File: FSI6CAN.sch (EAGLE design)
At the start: 32 parts, among them IC1 ATMEGA32M1, IC2 MCP2551

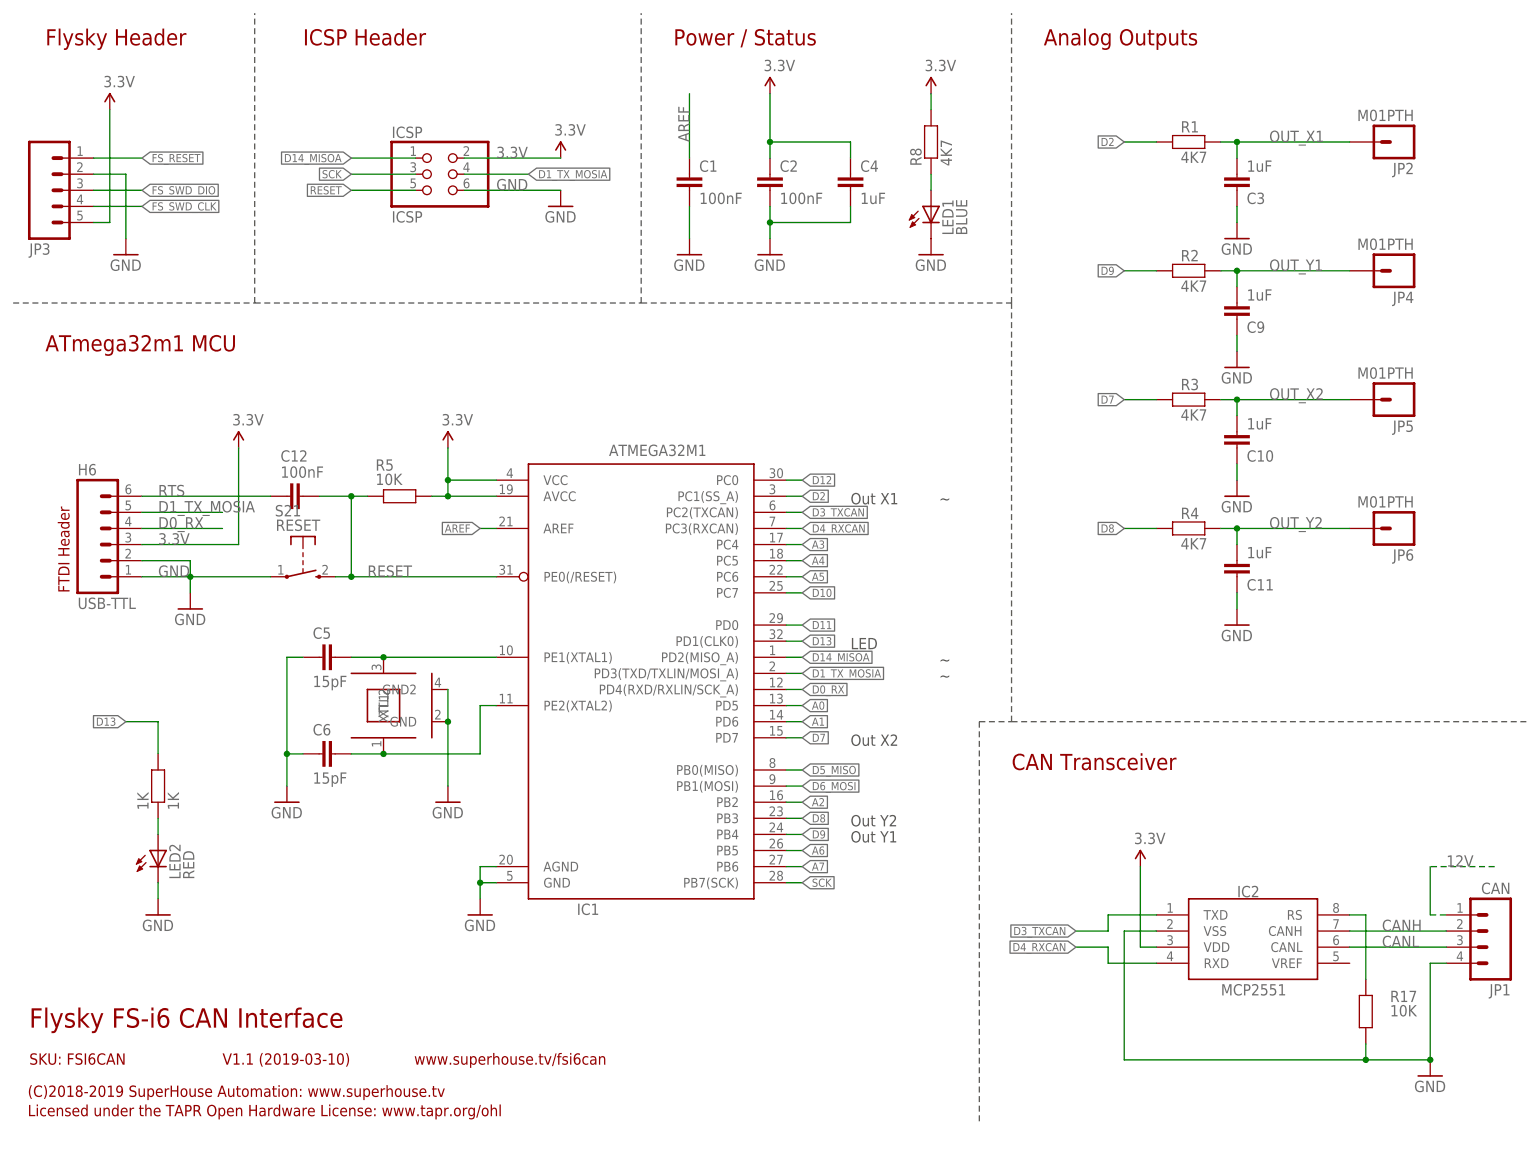
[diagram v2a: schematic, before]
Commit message: Added CAN termination
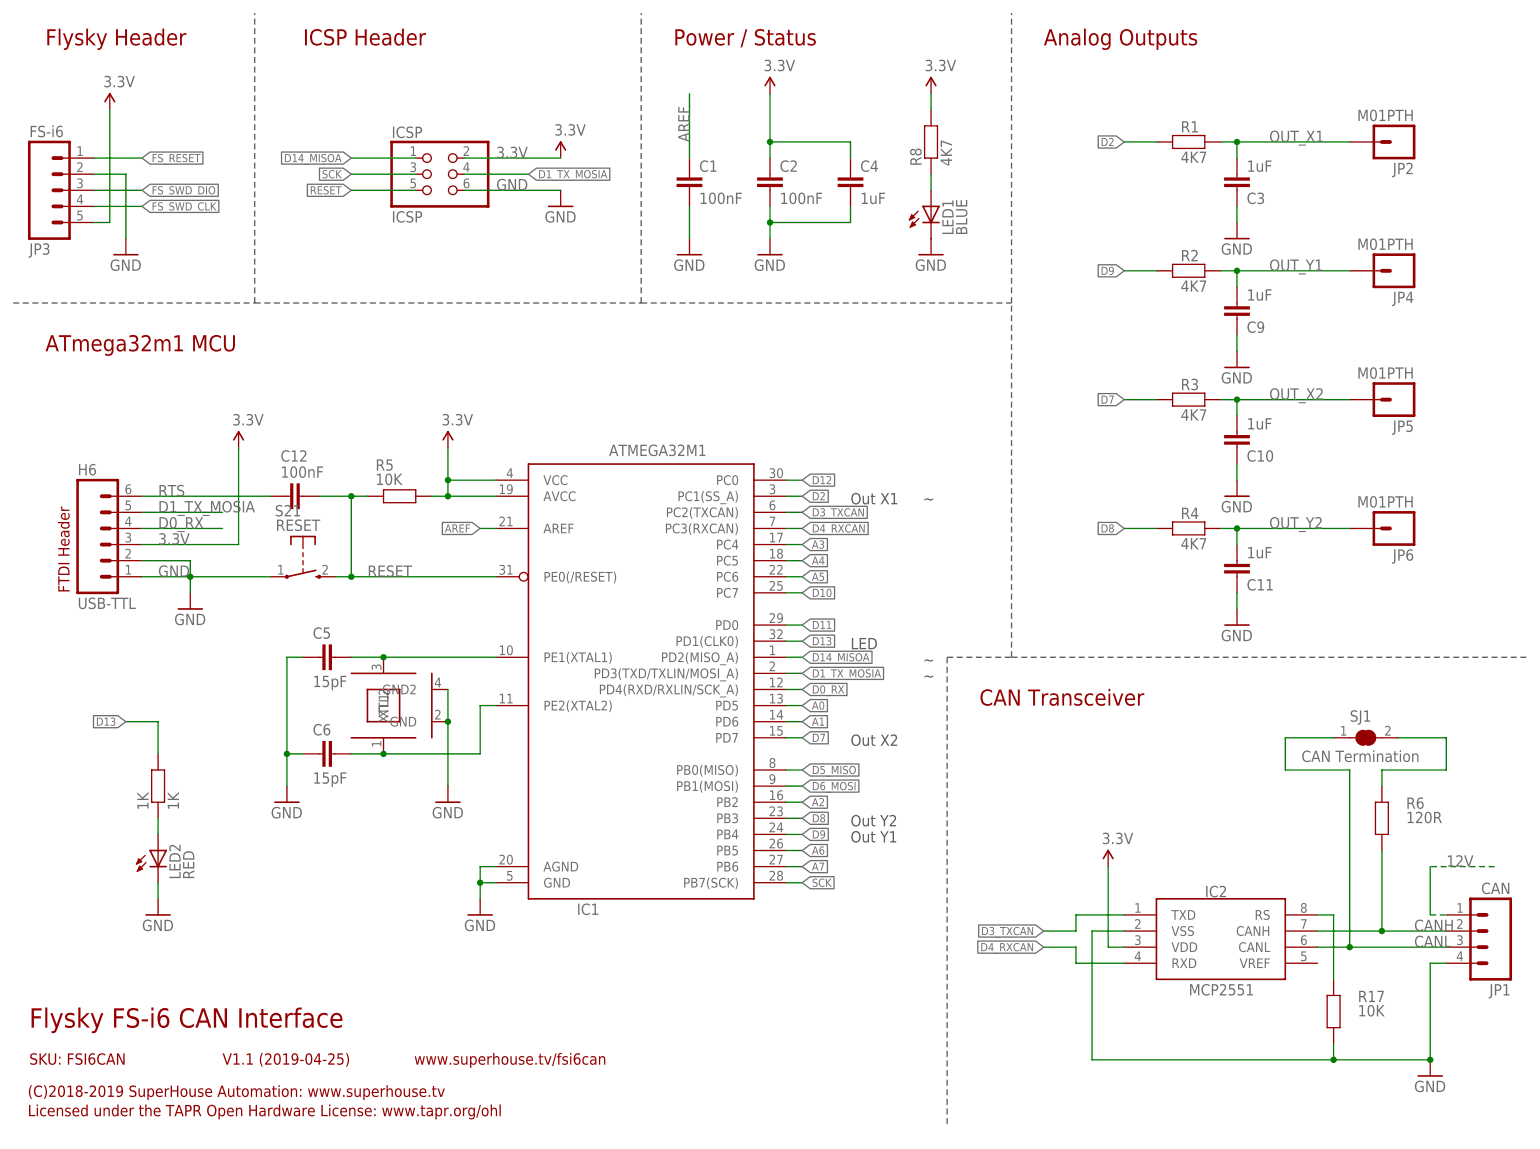
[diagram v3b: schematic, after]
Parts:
- added R6: 120R, freetronics-master-v1.1:RESISTOR0603
- added SJ1: CAN Termination, freetronics-jon:SJCN
- JP3: value (none) -> FS-i6
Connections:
- new net N$2: R6.2, SJ1.2
- net CANH: now also R6.1
- net CANL: now also SJ1.1
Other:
- note added: "V1.1 (2019-04-25)"
- note removed: "V1.1 (2019-03-10)"
- moved on the sheet: IC2, R17

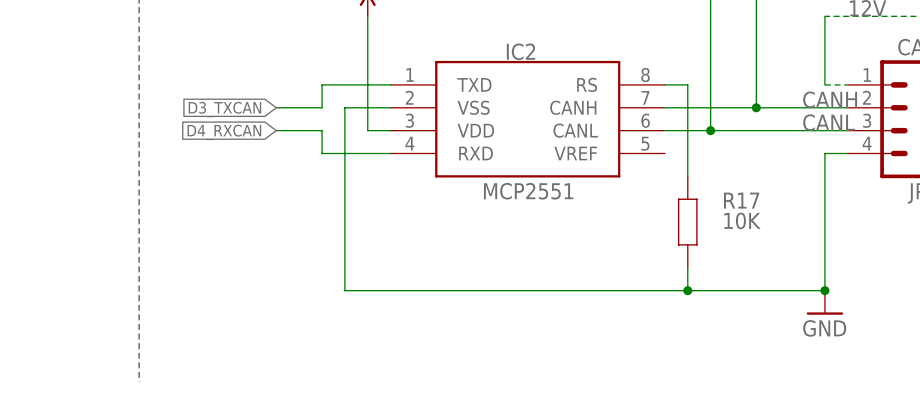
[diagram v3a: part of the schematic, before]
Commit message: Replaced MCP2551 with TCAN332DR
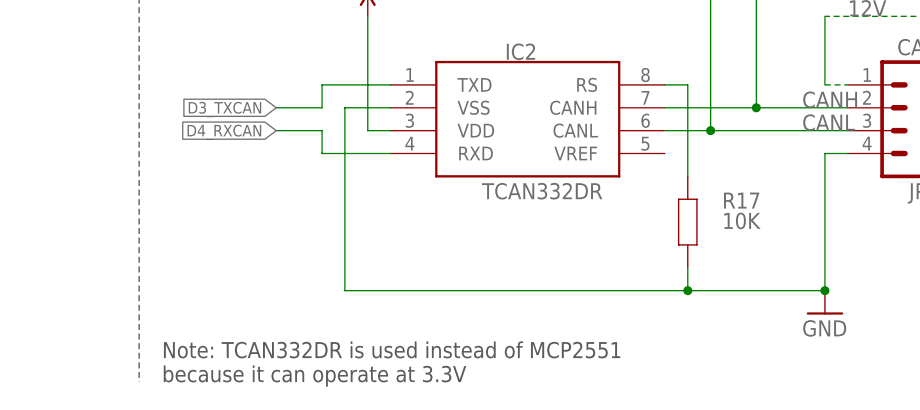
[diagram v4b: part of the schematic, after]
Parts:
- IC2: value MCP2551 -> TCAN332DR
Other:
- note added: "Note: TCAN332DR is used instead of MCP2551 because it can operate at 3.3V"
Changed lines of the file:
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@@
 <part name="R8" library="freetronics-jon" deviceset="RESISTOR" device="0603" value="4K7"/>
 <part name="LED1" library="freetronics-jon" deviceset="LED" device="0603" value="BLUE"/>
-<part name="IC2" library="freetronics-original" deviceset="MCP2551" device=""/>
+<part name="IC2" library="freetronics-original" deviceset="MCP2551" device="" value="TCAN332DR"/>
 <part name="R17" library="freetronics-master-v1.1" deviceset="RESISTOR" device="0603" value="10K"/>
 <part name="JP1" library="freetronics-jon" deviceset="M04" device="PTH" value="CAN"/>
@@
 <text x="137.16" y="49.53" size="1.778" layer="97">Out Y1</text>
 <text x="137.16" y="80.01" size="1.778" layer="97">LED</text>
+<text x="154.94" y="5.08" size="1.778" layer="97">Note: TCAN332DR is used instead of MCP2551
+because it can operate at 3.3V</text>
 </plain>
 <instances>
@@
 </drawing>
 <compatibility>
+<note version="6.3" minversion="6.2.2" severity="warning">
+Since Version 6.2.2 text objects can contain more than one line,
+which will not be processed correctly with this version.
+</note>
 <note version="8.2" severity="warning">
 Since Version 8.2, EAGLE supports online libraries. The ids

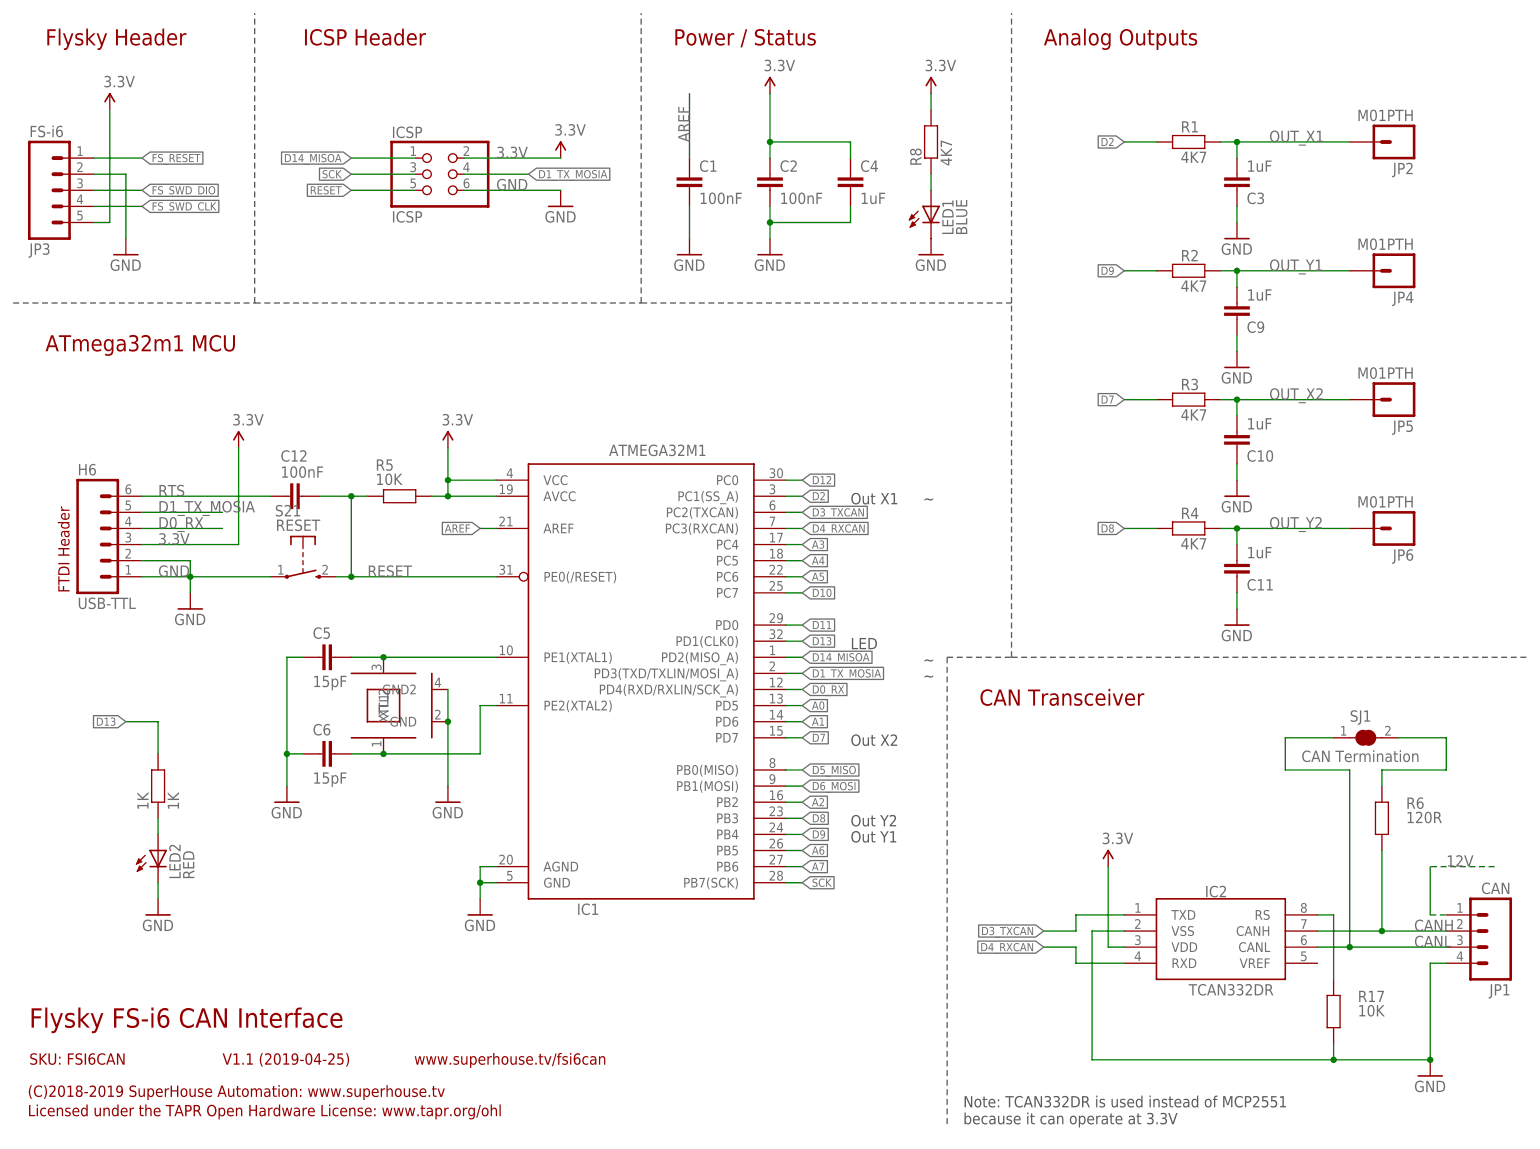
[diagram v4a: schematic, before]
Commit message: Major rework using ATmega328p and MCP2515 for v2.0 release
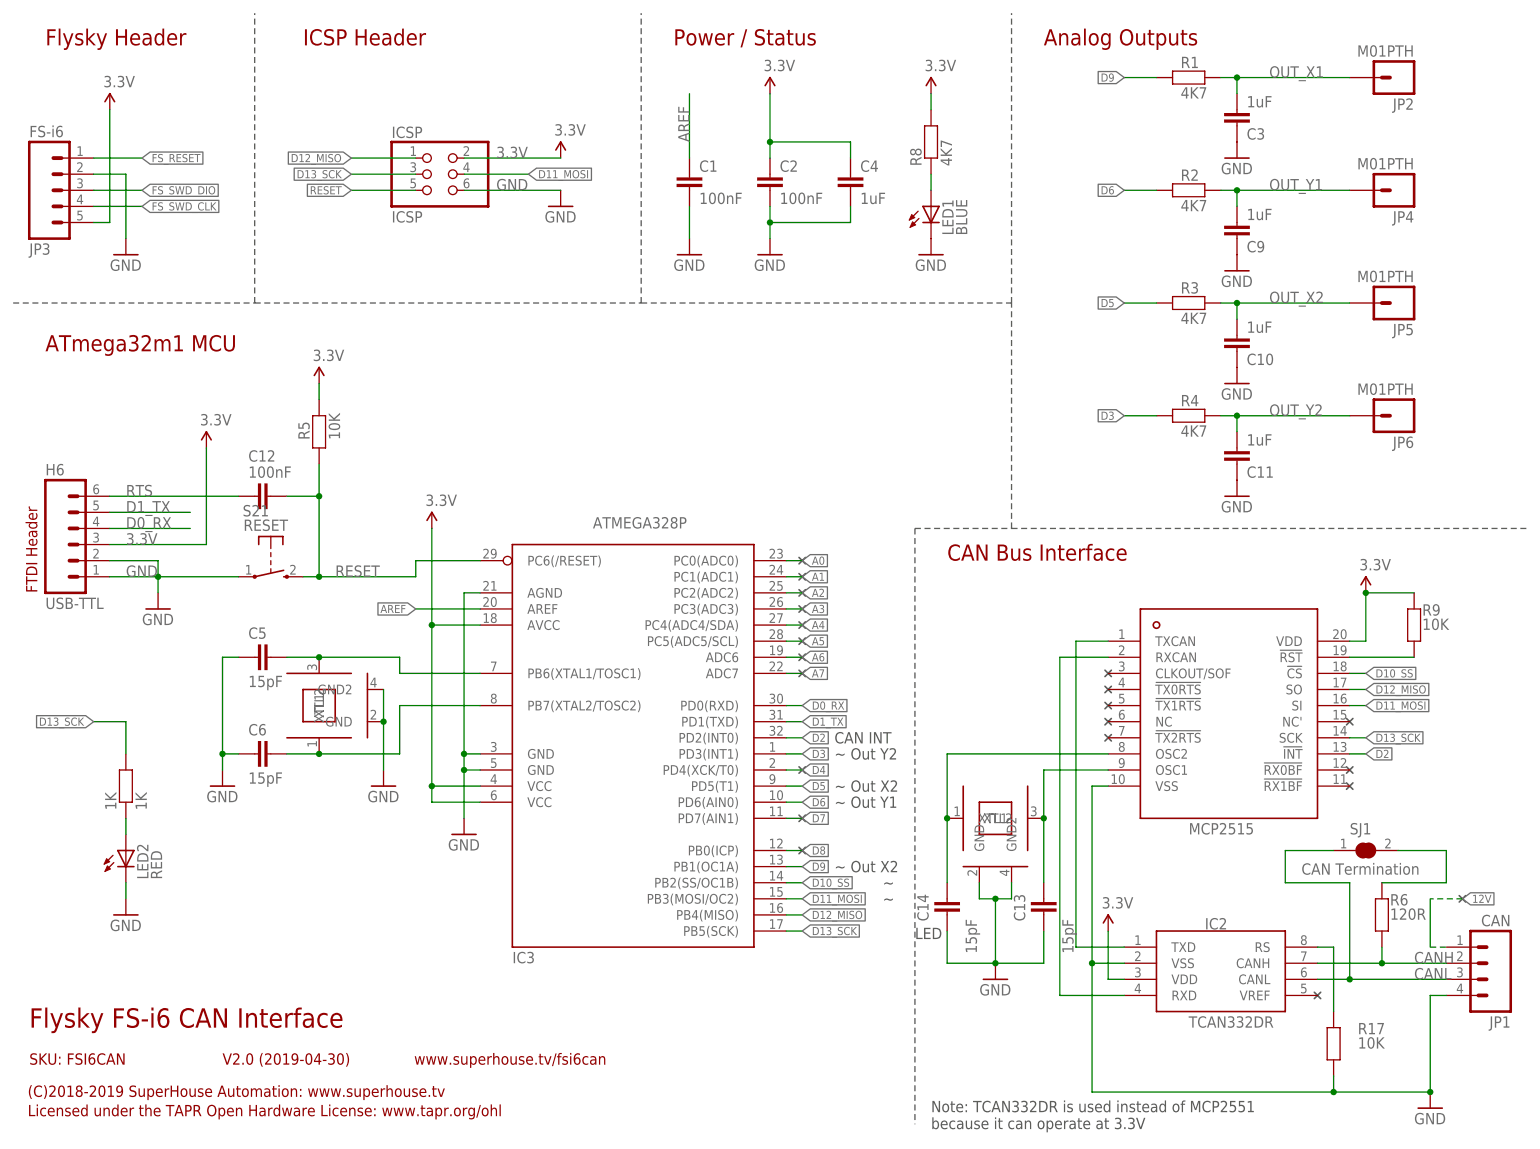
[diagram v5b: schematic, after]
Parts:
- removed IC1: ATMEGA32M1, freetronics-jon:ATMEGA32M1
- added C13, C14: 15pF, freetronics-master-v1.1:CAP0603
- added IC3: ATMEGA328P, freetronics-master-v1.1:AVR-MEGA8-AI
- added IC4: MCP2515, MCP2515:MCP2515
- added R9: 10K, freetronics-master-v1.1:RESISTOR0603
- added XTL3: 16MHz, freetronics-jon:CRYSTAL-GND3X2
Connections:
- removed net D10: IC1.PC7
- removed net D11: IC1.PD0
- removed net D12: IC1.PC0
- removed net D13: 1K.2, IC1.PD1(CLK0)
- removed net D14_MISOA: IC1.PD2(MISO_A), ICSP.1
- removed net D1_TX_MOSIA: H6.5, IC1.PD3(TXD/TXLIN/MOSI_A), ICSP.4
- removed net D3_TXCAN: IC1.PC2(TXCAN), IC2.TXD
- removed net D4_RXCAN: IC1.PC3(RXCAN), IC2.RXD
- removed net D5_MISO: IC1.PB0(MISO)
- removed net D6_MOSI: IC1.PB1(MOSI)
- removed net SCK: IC1.PB7(SCK), ICSP.3
- new net D10_SS: IC3.PB2(SS/OC1B), IC4.!CS
- new net D11_MOSI: IC3.PB3(MOSI/OC2), IC4.SI, ICSP.4
- new net D12_MISO: IC3.PB4(MISO), IC4.SO, ICSP.1
- new net D13_SCK: 1K.2, IC3.PB5(SCK), IC4.SCK, ICSP.3
- new net D1_TX: H6.5, IC3.PD1(TXD)
- new net D3: IC3.PD3(INT1), R4.1
- new net D4: IC3.PD4(XCK/T0)
- new net D5: IC3.PD5(T1), R3.1
- new net D6: IC3.PD6(AIN0), R2.1
- new net N$17: IC4.!RST, R9.1
- new net N$4: IC2.TXD, IC4.TXCAN
- new net N$6: IC2.RXD, IC4.RXCAN
- new net N$7: C13.2, IC4.OSC1, XTL3.XTL2
- new net N$8: C14.2, IC4.OSC2, XTL3.XTL1
- net 3.3V: now also IC3.AVCC, IC3.VCC@1, IC3.VCC@2, IC4.VDD, R9.2; no longer IC1.AVCC, IC1.VCC
- net A0: now also IC3.PC0(ADC0); no longer IC1.PD5
- net A1: now also IC3.PC1(ADC1); no longer IC1.PD6
- net A2: now also IC3.PC2(ADC2); no longer IC1.PB2
- net A3: now also IC3.PC3(ADC3); no longer IC1.PC4
- net A4: now also IC3.PC4(ADC4/SDA); no longer IC1.PC5
- net A5: now also IC3.PC5(ADC5/SCL); no longer IC1.PC6
- net A6: now also IC3.ADC6; no longer IC1.PB5
- net A7: now also IC3.ADC7; no longer IC1.PB6
- net AREF: now also IC3.AREF; no longer IC1.AREF
- net D0_RX: now also IC3.PD0(RXD); no longer IC1.PD4(RXD/RXLIN/SCK_A)
- net D2: now also IC3.PD2(INT0), IC4.!INT; no longer IC1.PC1(SS_A), R1.1
- net D7: now also IC3.PD7(AIN1); no longer IC1.PD7, R3.1
- net D8: now also IC3.PB0(ICP); no longer IC1.PB3, R4.1
- net D9: now also IC3.PB1(OC1A), R1.1; no longer IC1.PB4, R2.1
- net GND: now also C13.1, C14.1, IC3.AGND, IC3.GND@1, IC3.GND@2, IC4.VSS, XTL3.GND, XTL3.GND2; no longer IC1.AGND, IC1.GND
- net N$11: now also IC3.PB6(XTAL1/TOSC1); no longer IC1.PE1(XTAL1)
- net N$12: now also IC3.PB7(XTAL2/TOSC2); no longer IC1.PE2(XTAL2)
- net RESET: now also IC3.PC6(/RESET); no longer IC1.PE0(/RESET)
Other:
- note added: "CAN Bus Interface"
- note added: "CAN INT"
- note added: "V2.0 (2019-04-30)"
- note added: "~ Out X2"
- note added: "~ Out Y1"
- note added: "~ Out Y2"
- note removed: "CAN Transceiver"
- note removed: "Out X1"
- note removed: "Out X2"
- note removed: "Out Y1"
- note removed: "Out Y2"
- note removed: "V1.1 (2019-04-25)"
- moved on the sheet: 1K, C10, C11, C12, C3, C5, C6, C9, H6, IC2, JP1, JP2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
